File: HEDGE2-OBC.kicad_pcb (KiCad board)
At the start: 4 copper layers, 90.2 x 95.9 mm, 68 parts, among them J1 SMA-J-P-X-RA-TH1, U1 ADP7158ARDZ-3.3-R7, U10 MAX6633MSA_T, U3 TXS0102QDCURQ1, U4 INA260AIPWR, U5 INA260AIPWR, U6 SN65HVD1782QDRQ1, U7 SN65HVD1782QDRQ1, U8 TCAN1046AVDYYRQ1, U9 MAX6633MSA_T

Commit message: Layout complete
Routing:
- net /CAN_B_S: track 52.0 -> 50.8 mm
- net /UART_COMM_DIR: track 29.2 -> 28.5 mm
- net /CAN_B_L: track 24.8 -> 24.2 mm
- net /PI_nLED_Activity: track 48.4 -> 49.0 mm
- net GND: track 42.2 -> 41.9 mm, vias 13 -> 19
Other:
- board text added: "POWER"
- board text removed: "OBC"
- board text removed: "PWR"

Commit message: Final layout, submitted to DFM
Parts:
- C19, C20, JP1, JP2, R6, R7, U10, U9: moved to B.Cu
- moved U2 45.2 mm to (208.0, 175.9)
- moved R7 9.01 mm to (216.6, 141.2), turned to 180 degrees
- moved R6 8.97 mm to (216.6, 143.9), turned to 0 degrees
- moved JP1 5.38 mm to (213.1, 143.9), turned to 180 degrees
- moved JP2 5.38 mm to (213.1, 141.2), turned to 0 degrees
- moved C19 4.65 mm to (181.4, 133.7)
- moved C20 4.59 mm to (233.6, 143.7)
- moved U10 0.36 mm to (236.0, 148.4), turned to 180 degrees
- moved U9 0.35 mm to (183.9, 138.3), turned to 180 degrees
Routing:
- net +5V_MPU: track 71.3 -> 94.8 mm
- net Net-(Module1A-WiFi_nDisable): track 4.07 -> 19.0 mm, vias 0 -> 1
- net +5V_GNSS: track 61.2 -> 73.9 mm
- net Net-(Module1A-BT_nDisable): track 3.82 -> 15.8 mm, vias 0 -> 1
- net Net-(U2-ANT): track 20.5 -> 9.82 mm
- net /5V_PERM: track 7.62 -> 0.00 mm
- net /SDA0_3V3: track 62.9 -> 69.9 mm
- net /UART_D_RX: track 28.7 -> 34.9 mm
- net /SCL0_3V3: track 68.4 -> 73.2 mm
- net /UART_D_TX: track 35.3 -> 38.1 mm
- net /BATT: track 2.54 -> 0.00 mm
- added copper zone on B.Cu, net +3V3

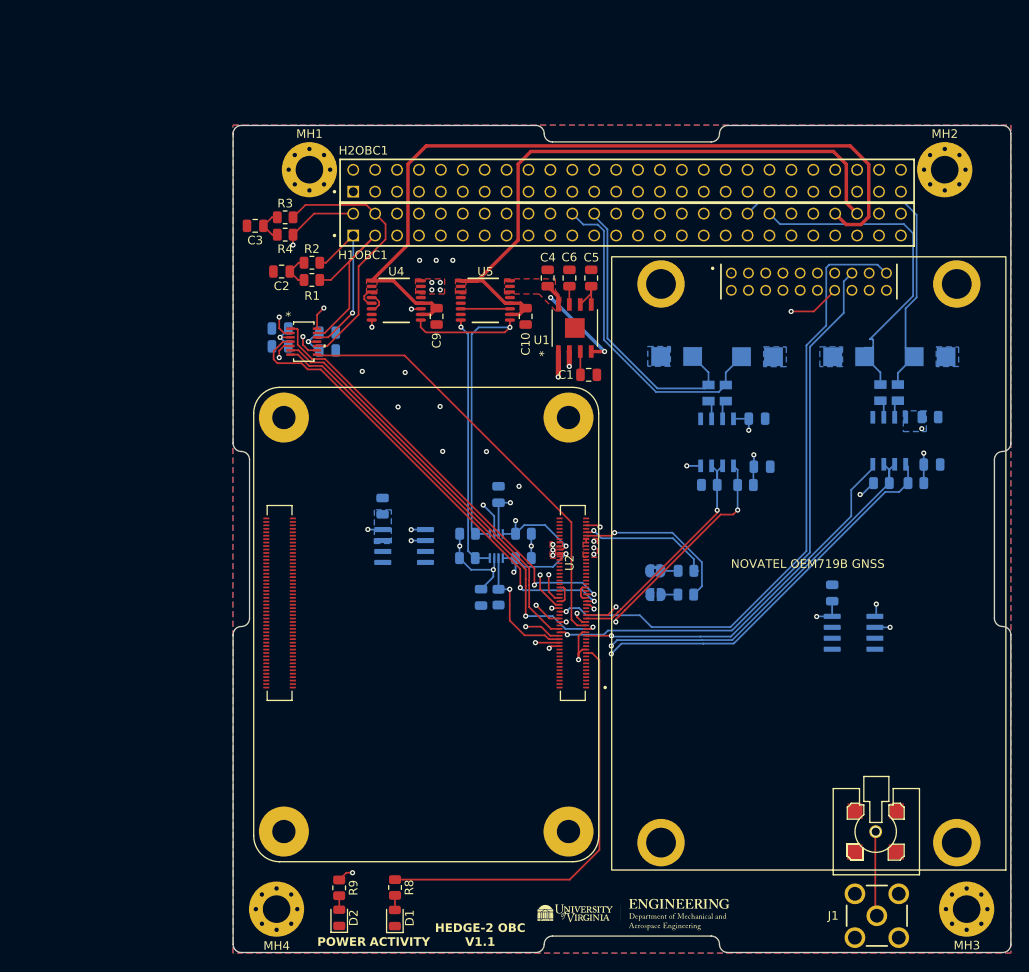
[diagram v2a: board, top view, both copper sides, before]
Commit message: Online DFM satisfactory
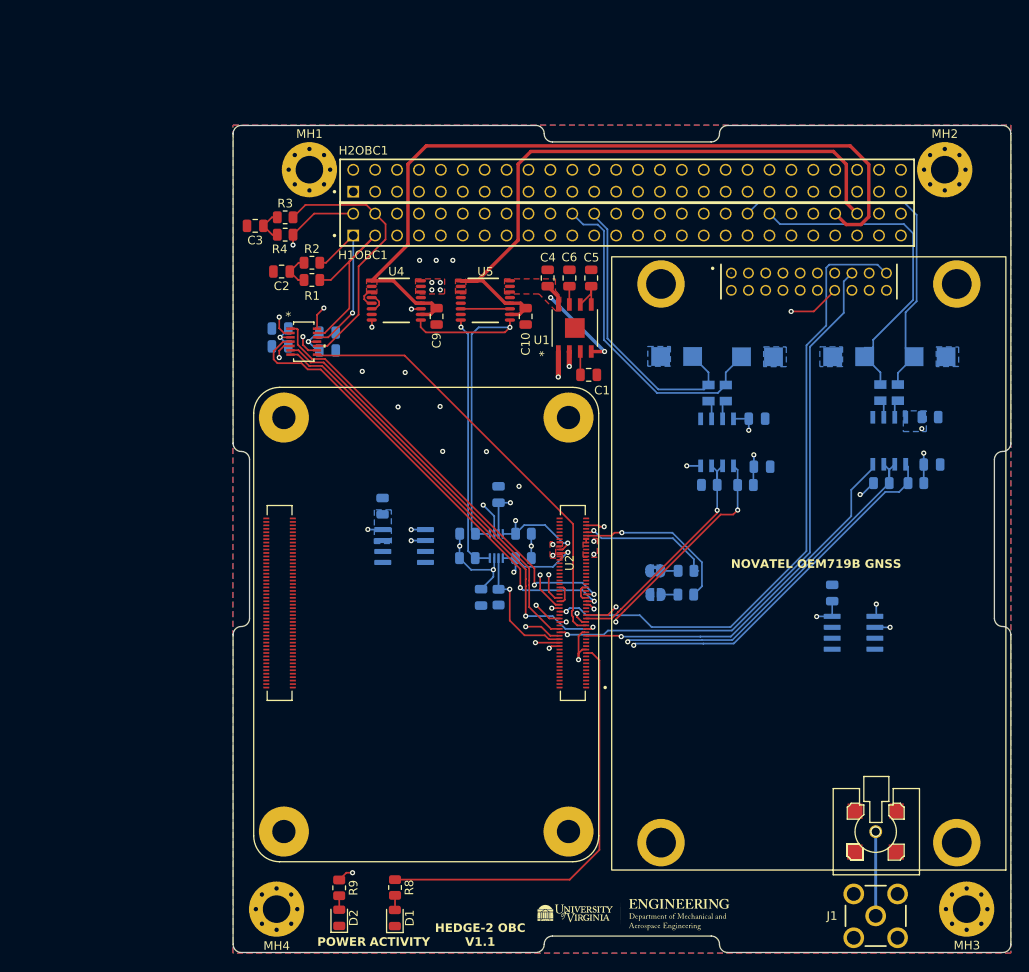
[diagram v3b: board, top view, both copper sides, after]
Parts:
- moved J1 0.14 mm to (238.6, 181.2)
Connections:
- net Net-(U2-ANT) renamed /Antenna
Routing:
- net /nPWR_LED: track 70.8 -> 71.5 mm
- net /UART_E_RX: track 39.3 -> 38.8 mm
- net +5V_CM4: vias 14 -> 13
- net +3V3: vias 8 -> 7

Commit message: Fix TCAN power supply swap
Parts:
- added G***: LOGO, HEDGE:HEDGE2-logo, B.Cu at (222.9, 161.8)
- C10, C9: value 0.1u -> 0u1
- C11, C12, C13, C14: value 100n -> 0u1
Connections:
- C15 pad 1: +3V3 -> +5V_CM4
- C16 pad 1: +3V3 -> +5V_CM4
- C17 pad 1: +5V_CM4 -> +3V3
- C18 pad 1: +5V_CM4 -> +3V3
- U8 pad 11: +5V_CM4 -> +3V3
- U8 pad 3: +3V3 -> +5V_CM4

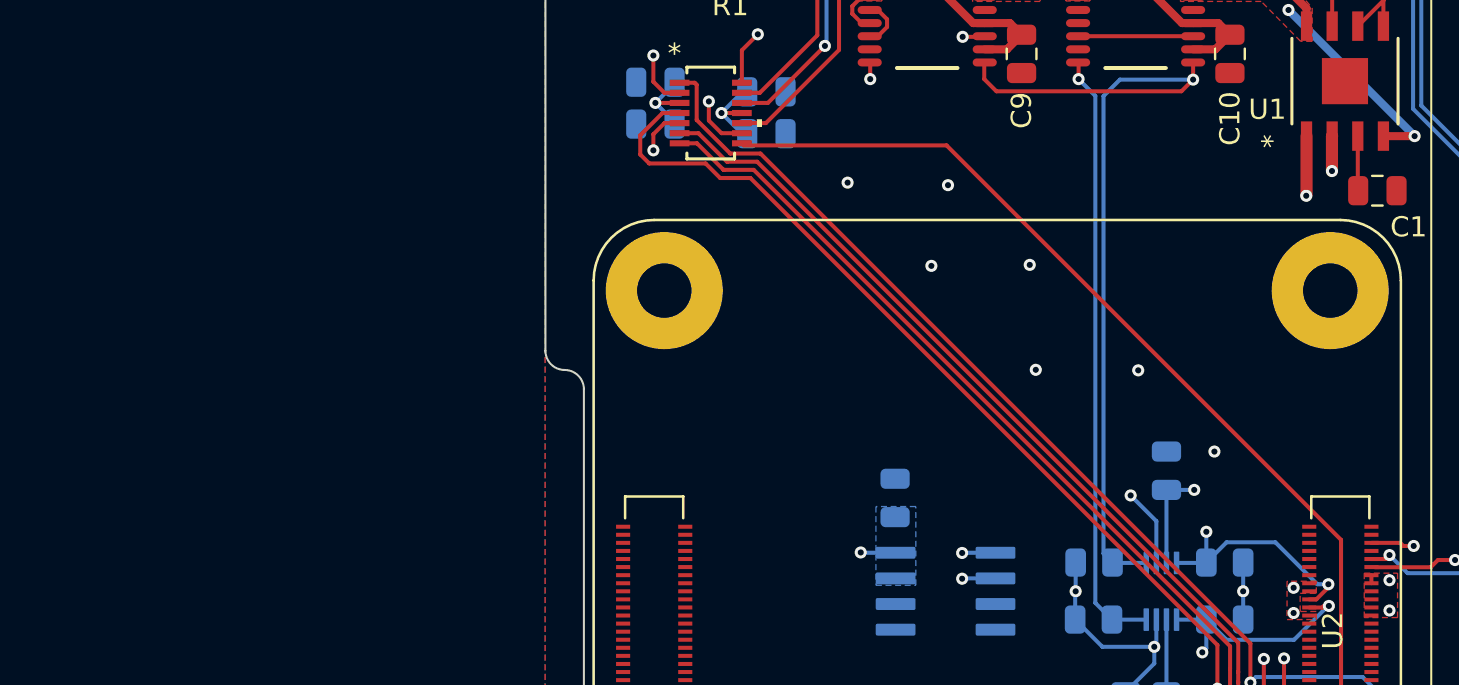
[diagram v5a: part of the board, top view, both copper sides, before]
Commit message: Add cap to 3V3 LDO output; add solder jumpers; change 3V3 routing
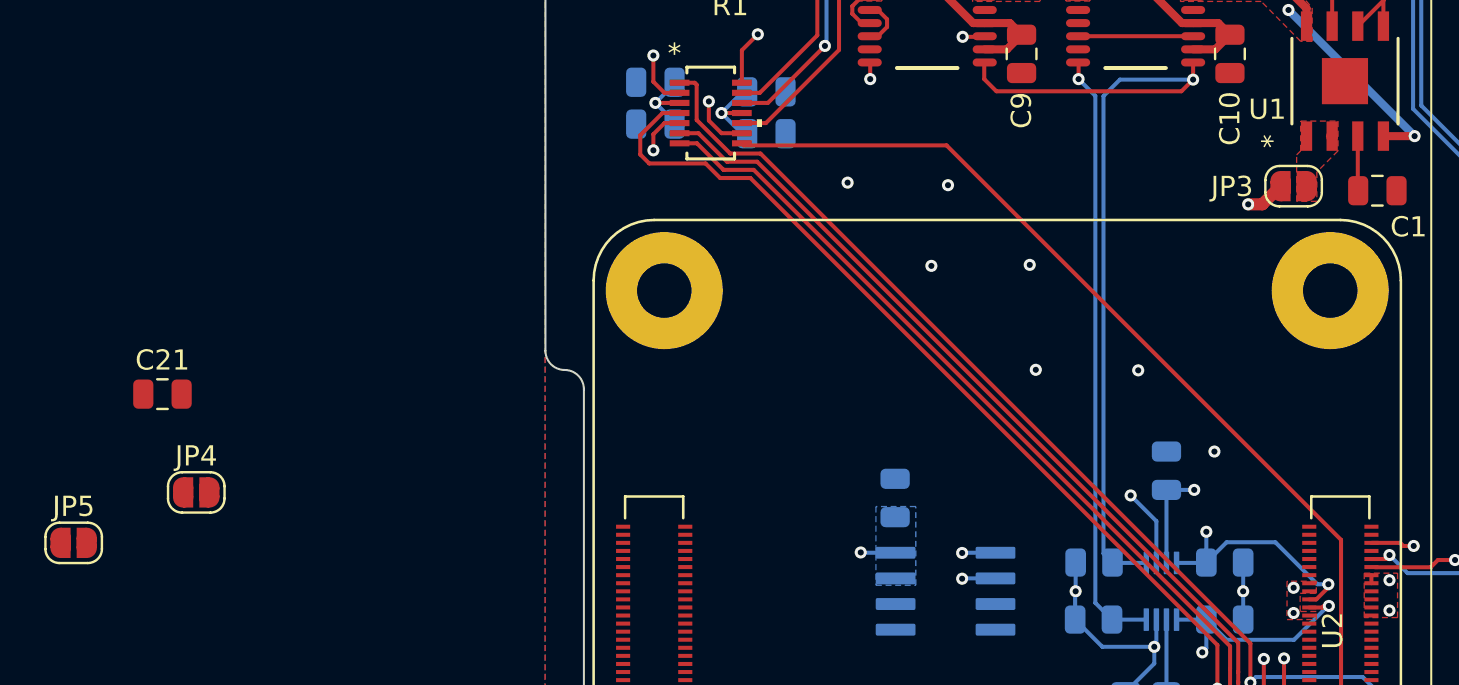
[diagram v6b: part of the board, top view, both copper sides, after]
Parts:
- added C21: 10u, Capacitor_SMD:C_0805_2012Metric, F.Cu at (145.1, 128.5)
- added JP3: OEM719B ENABLE, Jumper:SolderJumper-2_P1.3mm_Open_RoundedPad1.0x1.5mm, F.Cu at (201.2, 118.2)
- added JP4: LDO 3V3 ENABLE, Jumper:SolderJumper-2_P1.3mm_Open_RoundedPad1.0x1.5mm, F.Cu at (146.8, 133.4)
- added JP5: CM4 ENABLE, Jumper:SolderJumper-2_P1.3mm_Open_RoundedPad1.0x1.5mm, F.Cu at (140.7, 135.9)
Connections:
- U1 pad 1: +3V3_OEM719B -> Net-(JP3-A)
- U1 pad 2: +3V3_OEM719B -> Net-(JP3-A)
- U4 pad 14: +5V_CM4 -> /INA260_CM4/LOAD
- U4 pad 15: +5V_CM4 -> /INA260_CM4/LOAD
- U4 pad 16: +5V_CM4 -> /INA260_CM4/LOAD
- U5 pad 14: +5V_OEM719B -> /INA260_OEM719/LOAD
- U5 pad 15: +5V_OEM719B -> /INA260_OEM719/LOAD
- U5 pad 16: +5V_OEM719B -> /INA260_OEM719/LOAD
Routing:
- net +3V3_OEM719B: track 52.4 -> 30.3 mm, vias 2 -> 1
- added copper zone on F.Cu, net Net-(JP3-A)

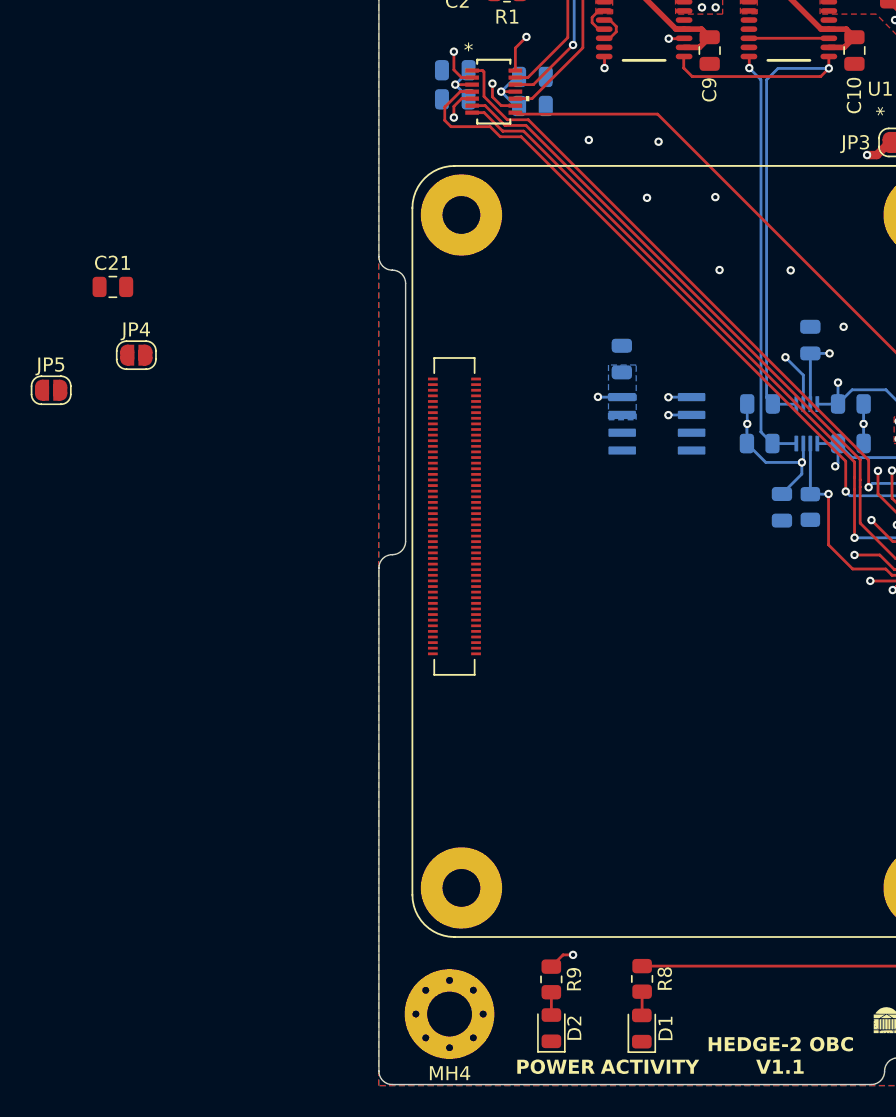
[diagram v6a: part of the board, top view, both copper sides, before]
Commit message: Fix solder mask on Pi connectors
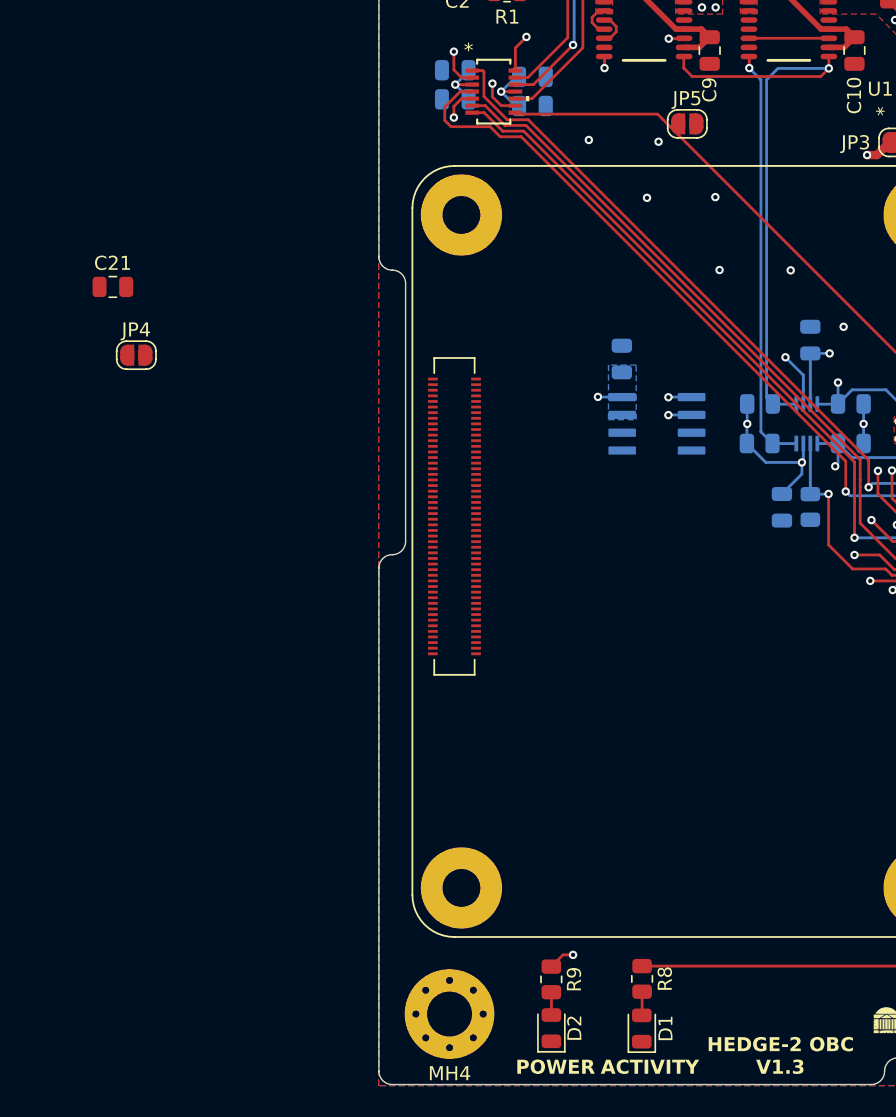
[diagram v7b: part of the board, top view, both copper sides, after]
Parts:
- moved JP5 49.2 mm to (186.1, 116.9)
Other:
- board text added: "HEDGE-2 OBC V1.3"
- board text removed: "HEDGE-2 OBC V1.1"
